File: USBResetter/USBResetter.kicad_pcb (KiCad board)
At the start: 2 copper layers, 43 x 20 mm, 12 parts, among them J1 USB In, J2 USB On, J3 USB Out, Q1 BC547, SW1 Bypass, U1 ASSR-1218

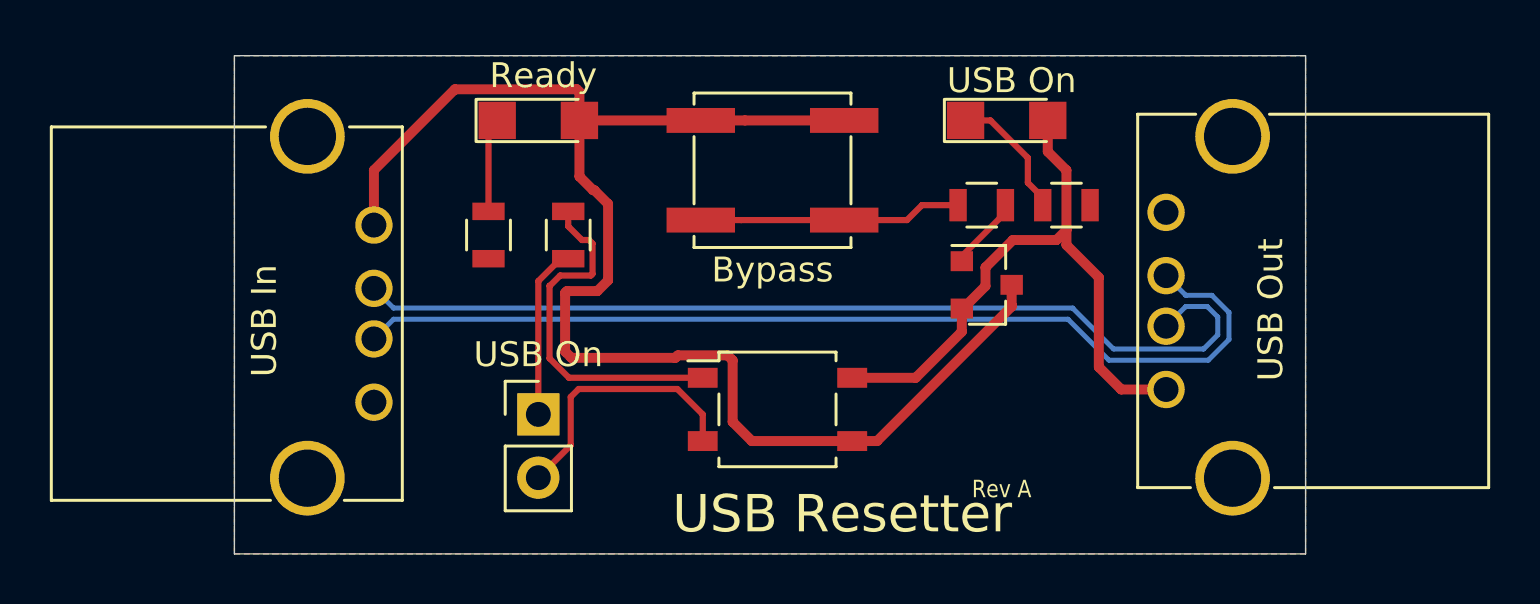
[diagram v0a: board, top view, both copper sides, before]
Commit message: Last Revision A update. (#7)
Fixed board dimensions issue
* Found one edge was short by 0.2mm.
* Fixed Board Dimension issue
* Board outline wasn't rendering correctly. Recreated the Edge Cuts layer
Bypass LED, Button Centered
* Added Bypass LED Indicator LED.
* Moved the Bypass button to center of the board.
* Simpliflied the ground plane.
Properly annotated schematic
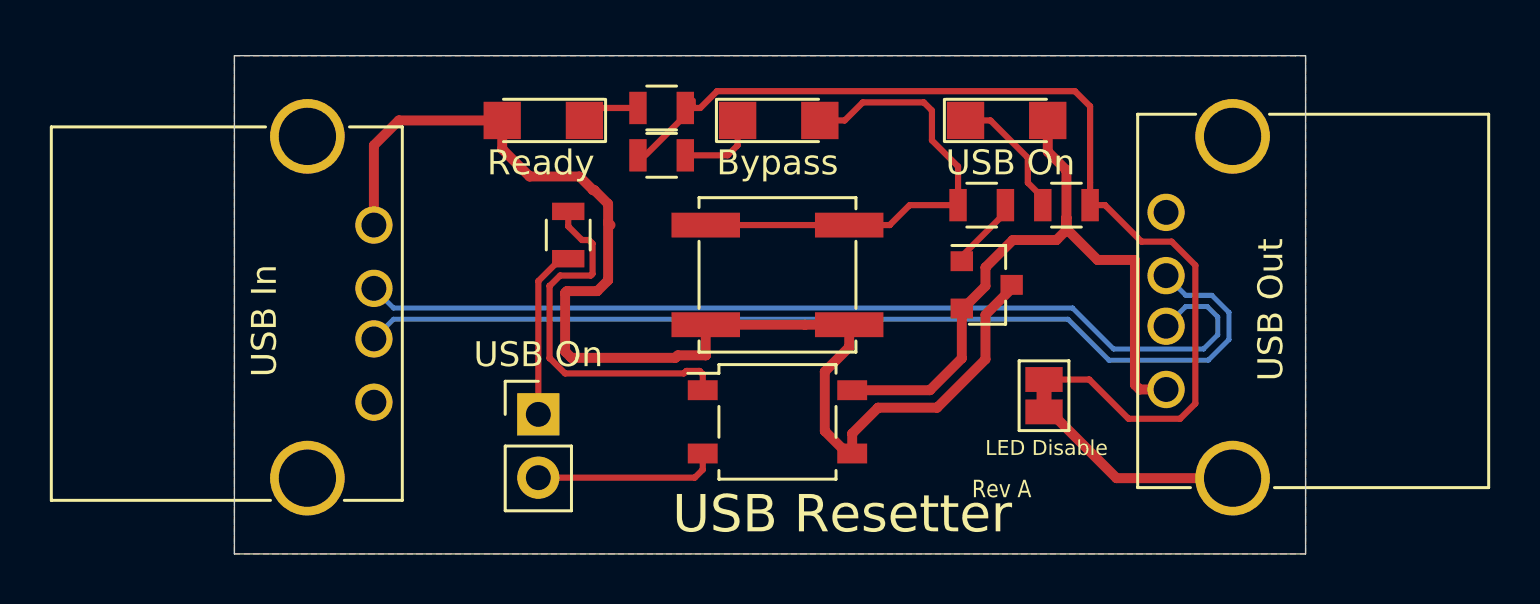
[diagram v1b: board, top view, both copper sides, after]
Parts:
- added D3: Bypass, LEDs:LED_1206, F.Cu at (146.8, 86.6)
- added JP1: LED Disable, Jumpers:SolderJumper-2_P1.3mm_Bridged_Pad1.0x1.5mm, F.Cu at (157.5, 97.7)
- added R5: 2K, Resistors_SMD:R_0805, F.Cu at (142.2, 88.0)
- Q1: value BC547 -> SS8050
- R1: value 500 -> 820
- moved R2 8.62 mm to (142.2, 86.1), turned to 180 degrees
- moved SW1 4.20 mm to (146.8, 92.8), turned to 180 degrees
- moved U1 0.50 mm to (146.8, 98.7)
- moved D1 0.20 mm to (137.4, 86.6), turned to 180 degrees
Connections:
- net Net-(R4-Pad1) renamed LED_Bypass
- R2 pad 1: GND -> Net-(JP1-Pad1)
- R3 pad 1: GND -> Net-(JP1-Pad1)
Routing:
- net Net-(JP1-Pad1): track 0.00 -> 41.5 mm
- net LED_Bypass: track 10.6 -> 19.6 mm
- net GND: track 0.00 -> 8.67 mm
- net VBUS: track 59.1 -> 52.8 mm
- net Net-(J2-Pad2): track 10.7 -> 7.38 mm
- net Net-(D3-Pad1): track 0.00 -> 3.27 mm
- net Bypass: track 25.9 -> 27.6 mm
- net Net-(D1-Pad1): track 3.79 -> 2.36 mm
- net Net-(R1-Pad2): track 14.4 -> 15.1 mm
